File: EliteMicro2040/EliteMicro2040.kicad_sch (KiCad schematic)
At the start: 40 parts, among them J2 Button, U101 WL2810D33-4/TR, U2 Elite-C, U3 RP2040, Y1 2016_4P

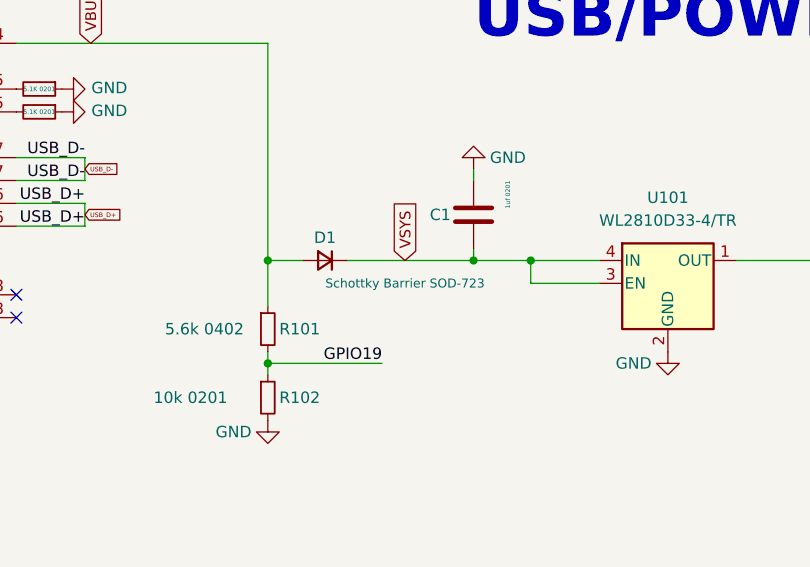
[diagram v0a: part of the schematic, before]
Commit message: small change to one value to autofill
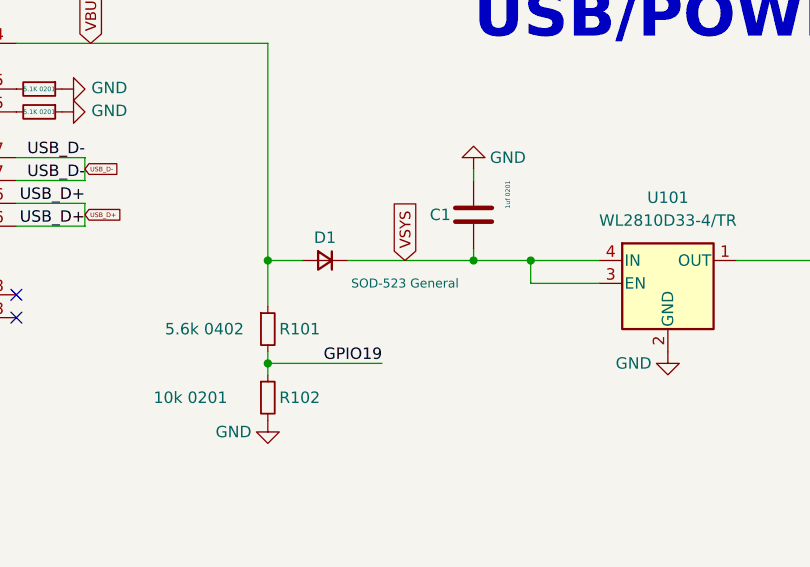
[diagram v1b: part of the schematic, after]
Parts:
- D1: value Schottky Barrier SOD-723 -> SOD-523 General
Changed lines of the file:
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@@
     (in_bom yes) (on_board yes)
     (property "Reference" "D1" (id 0) (at 74.93 41.91 0))
-    (property "Value" "Schottky Barrier SOD-723" (id 1) (at 83.82 46.99 0)
+    (property "Value" "SOD-523 General" (id 1) (at 83.82 46.99 0)
       (effects (font (size 1 1)))
     )
@@
     )
     (path "/05df6570-e64a-476d-93c7-a010dc147366"
-      (reference "D1") (unit 1) (value "Schottky Barrier SOD-723") (footprint "Diode_SMD:D_SOD-523")
+      (reference "D1") (unit 1) (value "SOD-523 General") (footprint "Diode_SMD:D_SOD-523")
     )
     (path "/00000000-0000-0000-0000-0000608edada"

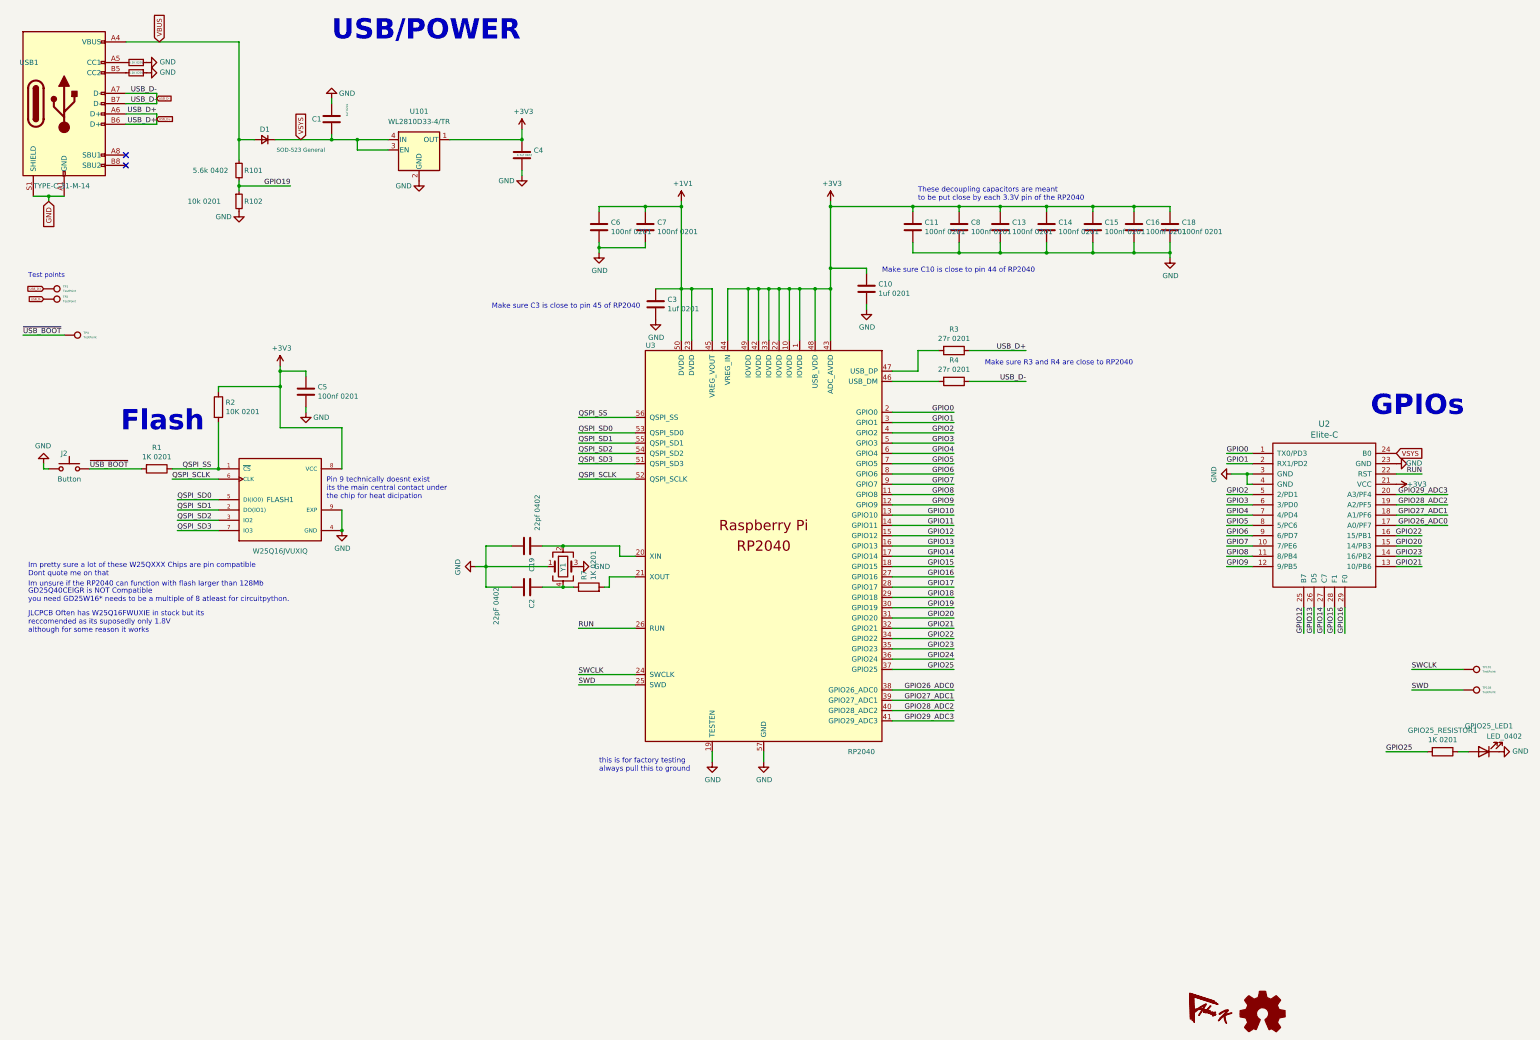
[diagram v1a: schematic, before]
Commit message: swapped regulator to sot-23-3 version
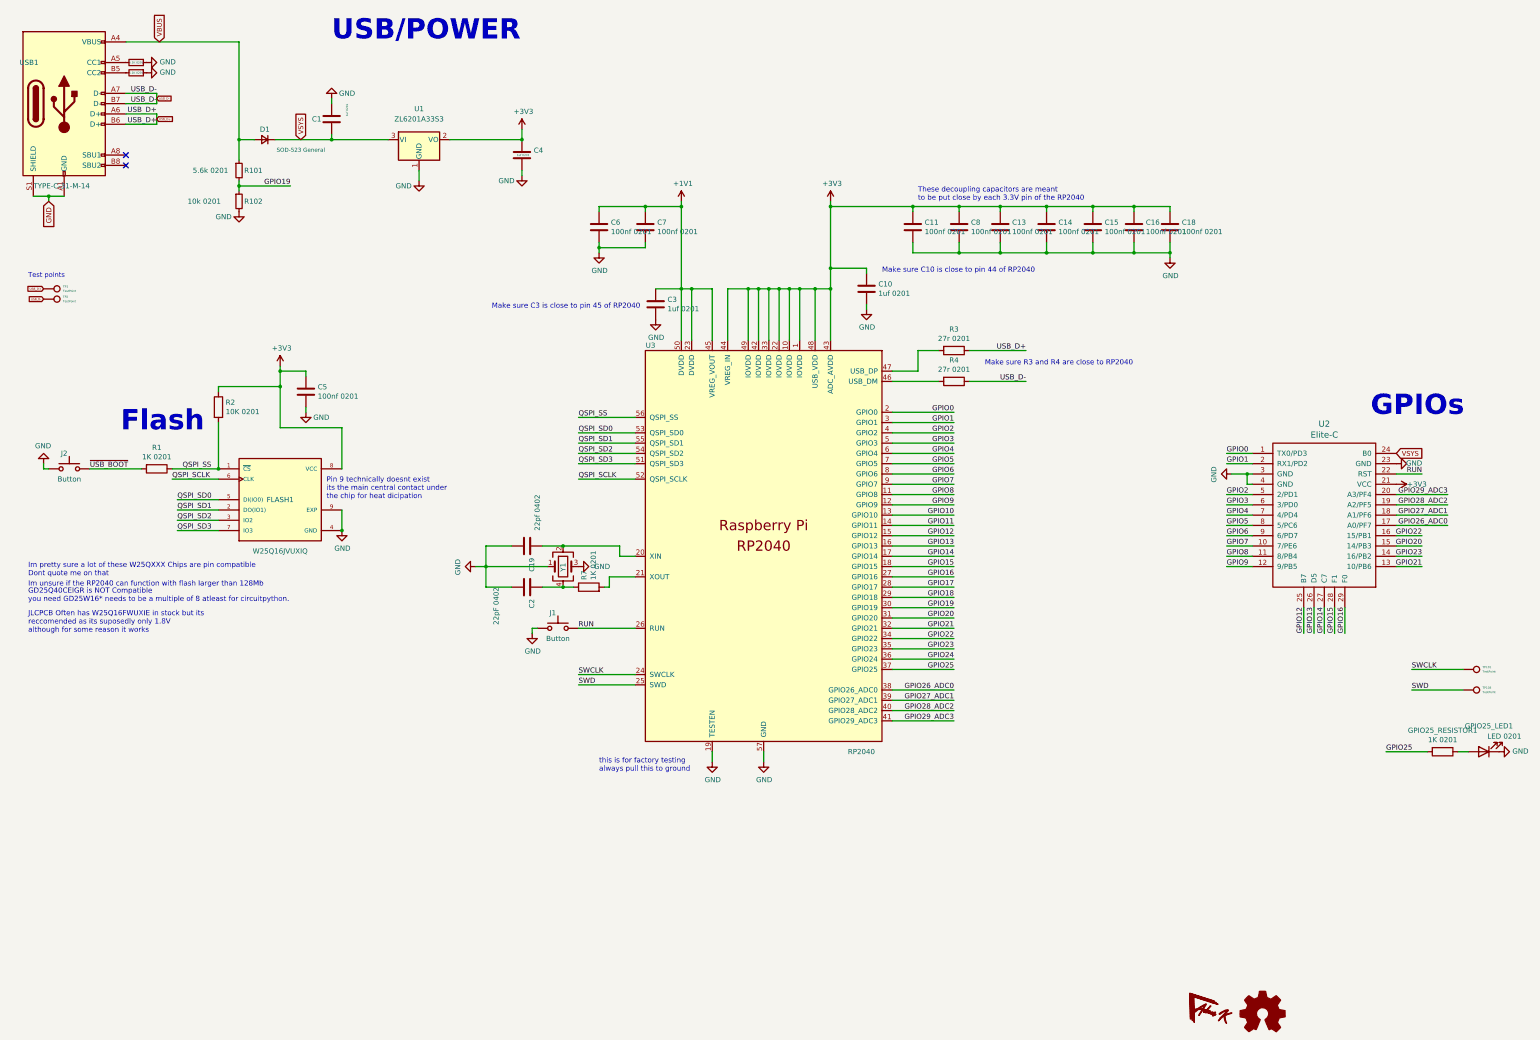
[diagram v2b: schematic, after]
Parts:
- removed TP4: TestPoint, EnvExtras:CustomTestPoint, symbol Connector:TestPoint
- removed U101: WL2810D33-4/TR, Package_DFN_QFN:UDFN-4-1EP_1x1mm_P0.65mm_EP0.48x0.48mm, symbol Regulator_Linear:TLV70033_WSON6
- added J1: Button, Button_Switch_SMD:SW_SPST_CK_KXT3, symbol Switch:SW_Push
- added U1: ZL6201A33S3, Package_TO_SOT_SMD:SOT-23, symbol Regulator_Linear:XC6206PxxxMR
- C4: value 4.7uf 0402 -> 1uf 0201; footprint Capacitor_SMD:C_0402_1005Metric -> Capacitor_SMD:C_0201_0603Metric
- GPIO25_LED1: value LED_0402 -> LED 0201; footprint LED_SMD:LED_0402_1005Metric -> LED_SMD:LED_0201_0603Metric
- R101: value 5.6k 0402 -> 5.6k 0201; footprint Resistor_SMD:R_0402_1005Metric -> Resistor_SMD:R_0201_0603Metric
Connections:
- net +3V3: now also U1.2 (VO)
- net GND: now also J1.2, U1.1 (GND)
- net RUN: now also J1.1
- net VSYS: now also U1.3 (VI)

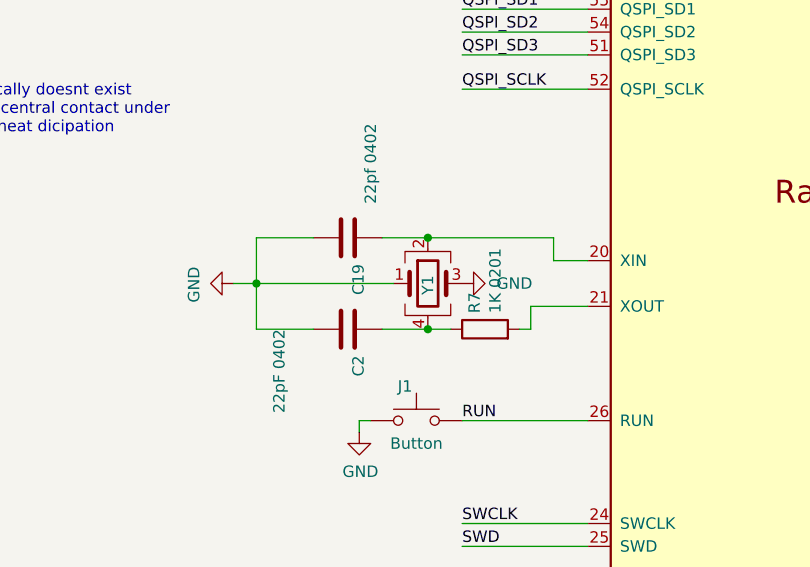
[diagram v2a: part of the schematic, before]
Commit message: swapped crystal for 3225 version
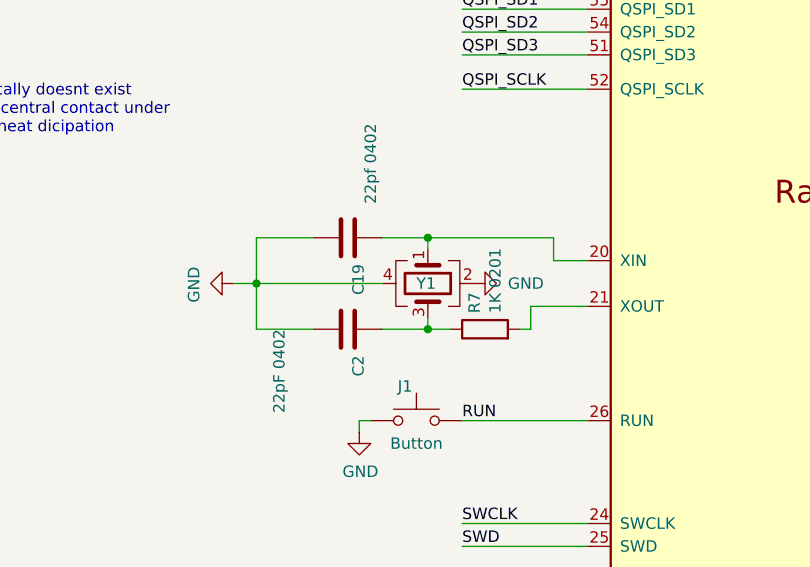
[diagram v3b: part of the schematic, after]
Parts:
- Y1: value 2016_4P -> 3225-4P; footprint Crystal:Crystal_SMD_2016-4Pin_2.0x1.6mm -> Crystal:Crystal_SMD_3225-4Pin_3.2x2.5mm
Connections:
- net GND: now also Y1.2, Y1.4; no longer Y1.1, Y1.3
- net at C19.1, U3.20 (XIN): now also Y1.1; no longer Y1.2
- net at C2.1, R7.1: now also Y1.3; no longer Y1.4
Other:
- moved on the sheet: Y1

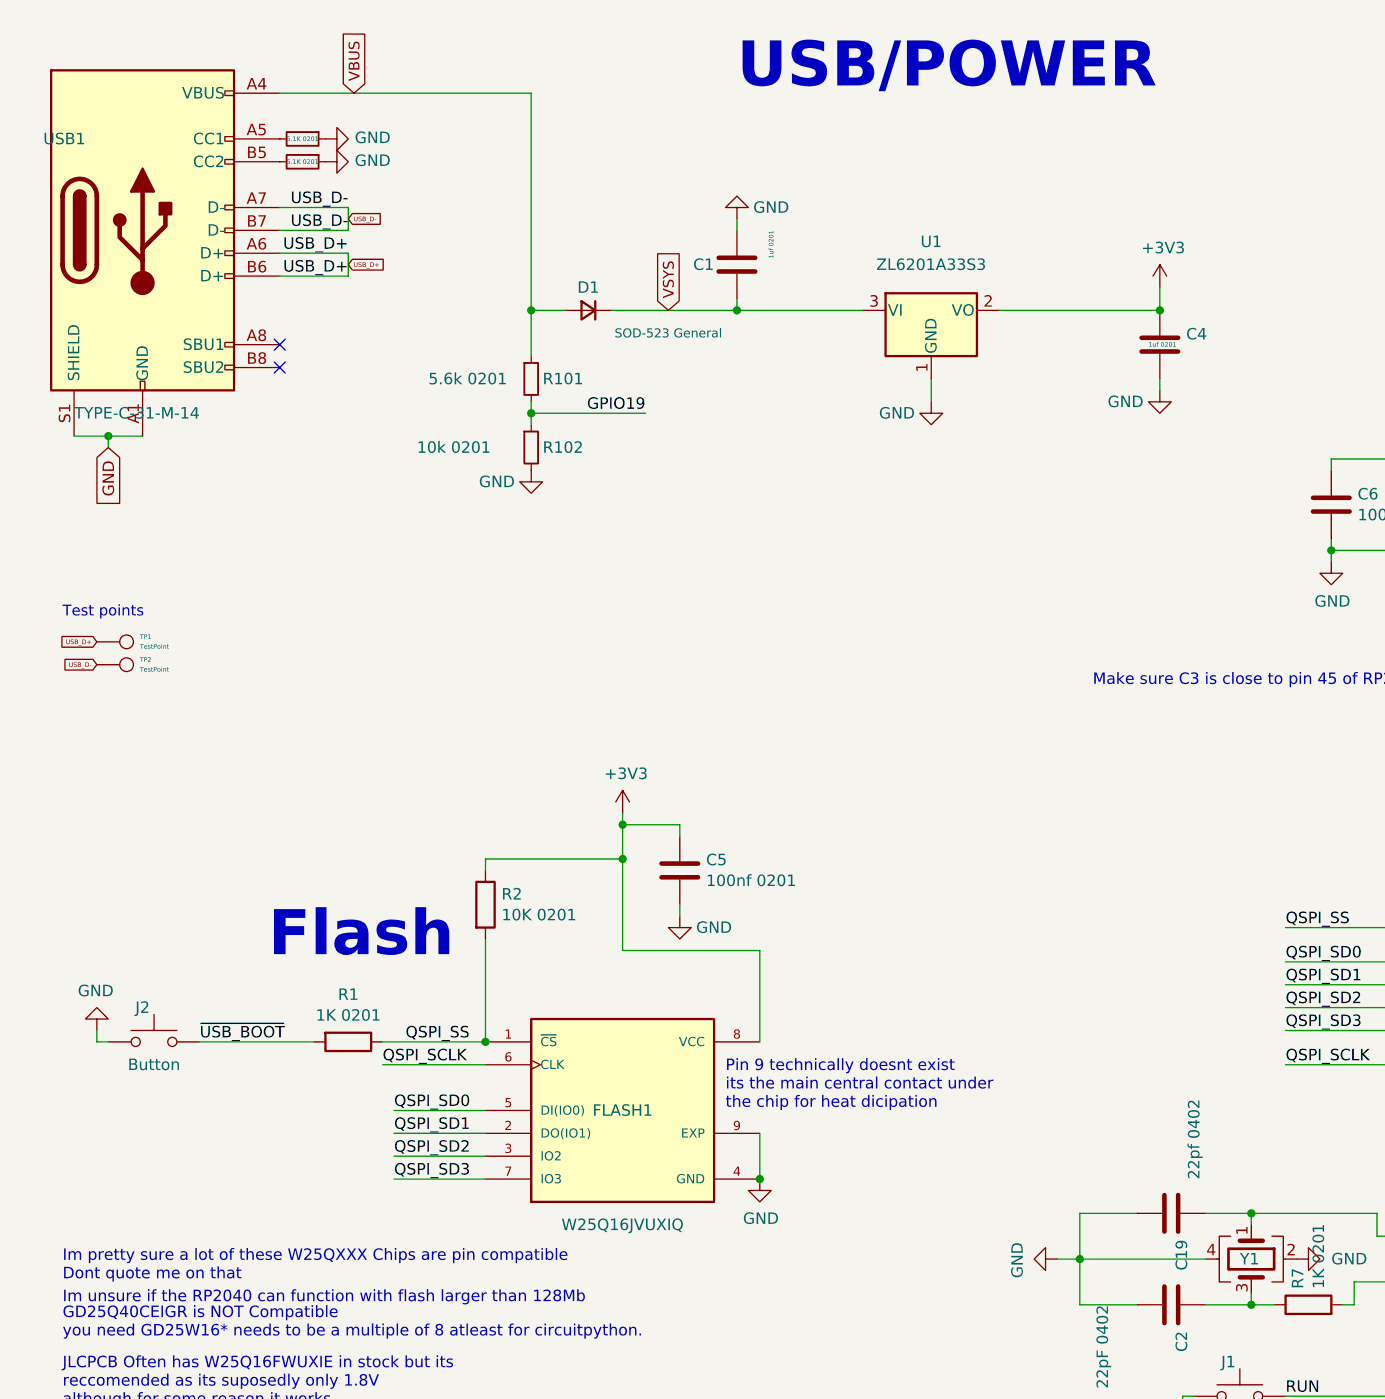
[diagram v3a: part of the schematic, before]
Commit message: replaced flash symbol with built in one, some clearance fixes
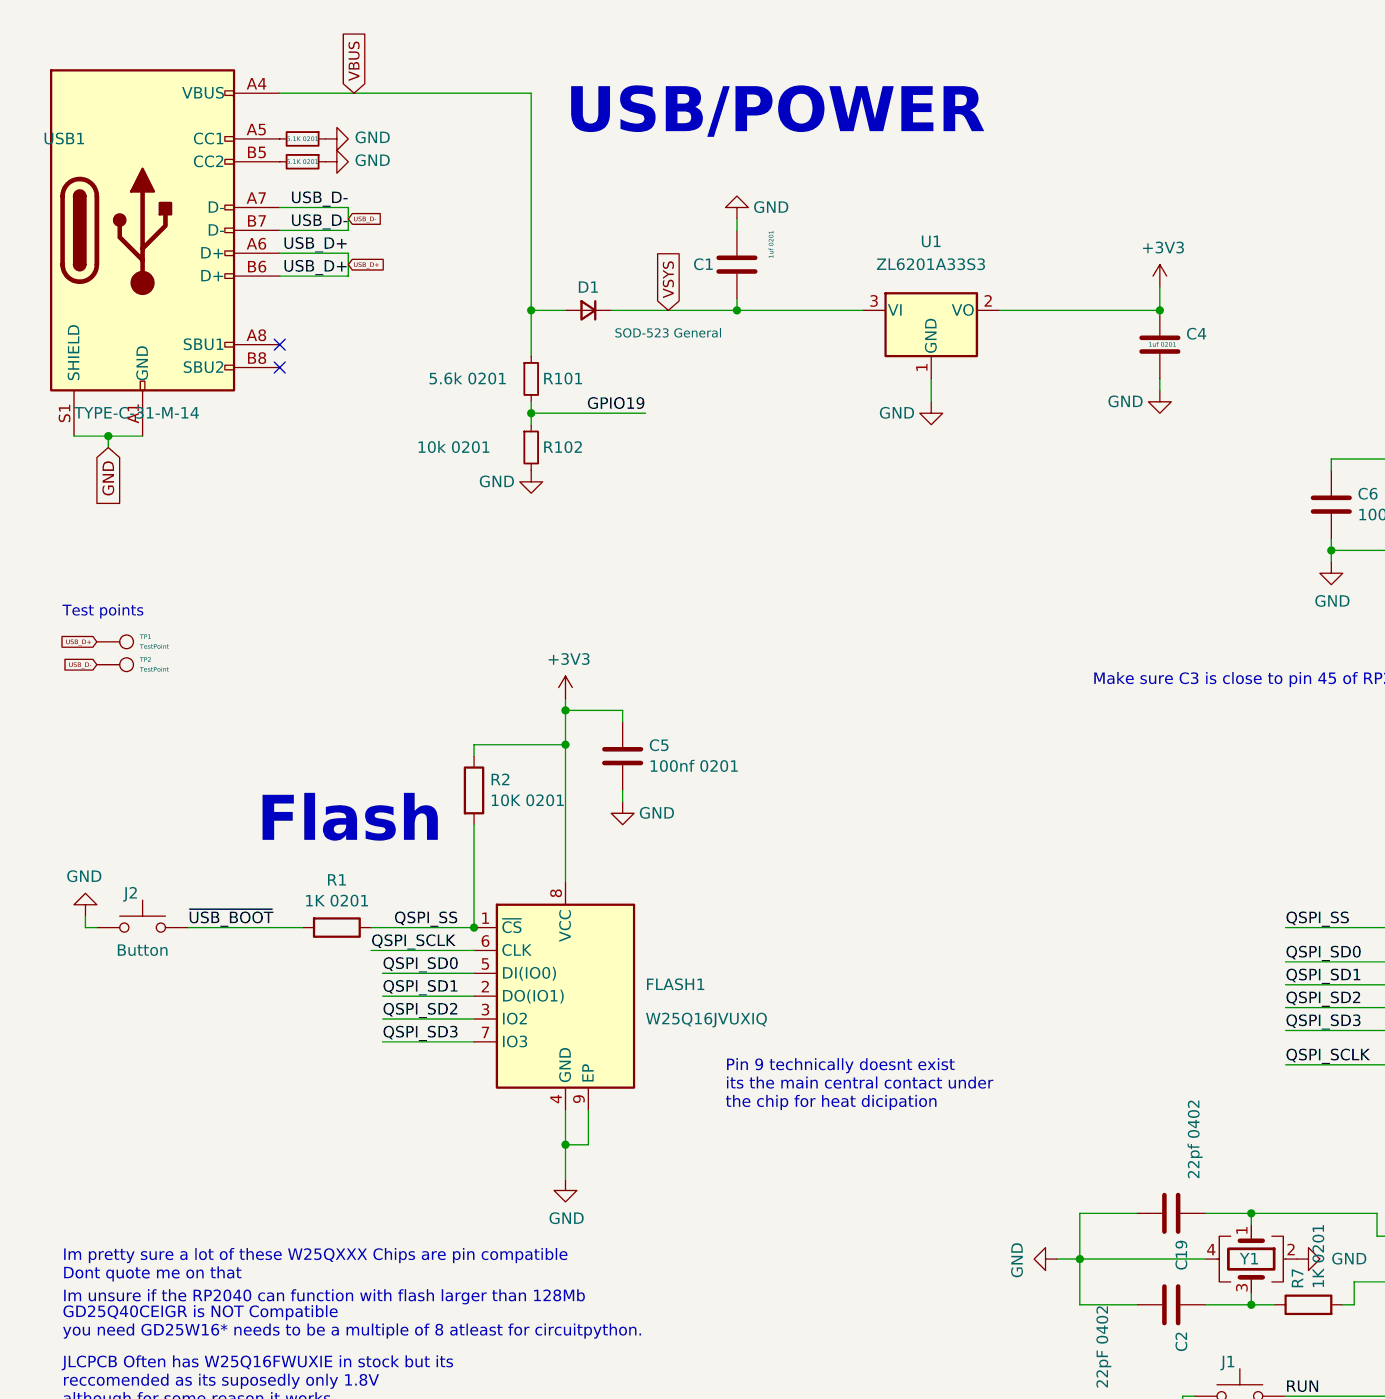
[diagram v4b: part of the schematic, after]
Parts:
- removed FLASH1: W25Q16JVUXIQ, Package_SON:SON-8-1EP_3x2mm_P0.5mm_EP1.4x1.6mm, symbol W25Q256JVEIQ_TR:W25Q256JVEIQ_TR
- added FLASH1: W25Q16JVUXIQ, Package_SON:SON-8-1EP_3x2mm_P0.5mm_EP1.4x1.6mm, symbol Memory_Flash:W25Q32JVZP
- Y1: value 3225-4P -> 3225-4P 12MHz
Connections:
- net +3V3: now also FLASH1.8 (VCC)
- net GND: now also FLASH1.4 (GND), FLASH1.9 (EP)
- net QSPI_SCLK: now also FLASH1.6 (CLK)
- net QSPI_SD0: now also FLASH1.5 (DI(IO0))
- net QSPI_SD1: now also FLASH1.2 (DO(IO1))
- net QSPI_SD2: now also FLASH1.3 (IO2)
- net QSPI_SD3: now also FLASH1.7 (IO3)
- net QSPI_SS: now also FLASH1.1 (~{CS})
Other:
- moved on the sheet: C5, J2, R1, R2
